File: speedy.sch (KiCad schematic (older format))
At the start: 42 parts, among them SW1 DFU, U1 STM32F415RGT6, U2 NUF2042VX6, X1 16Mhz 10ppm

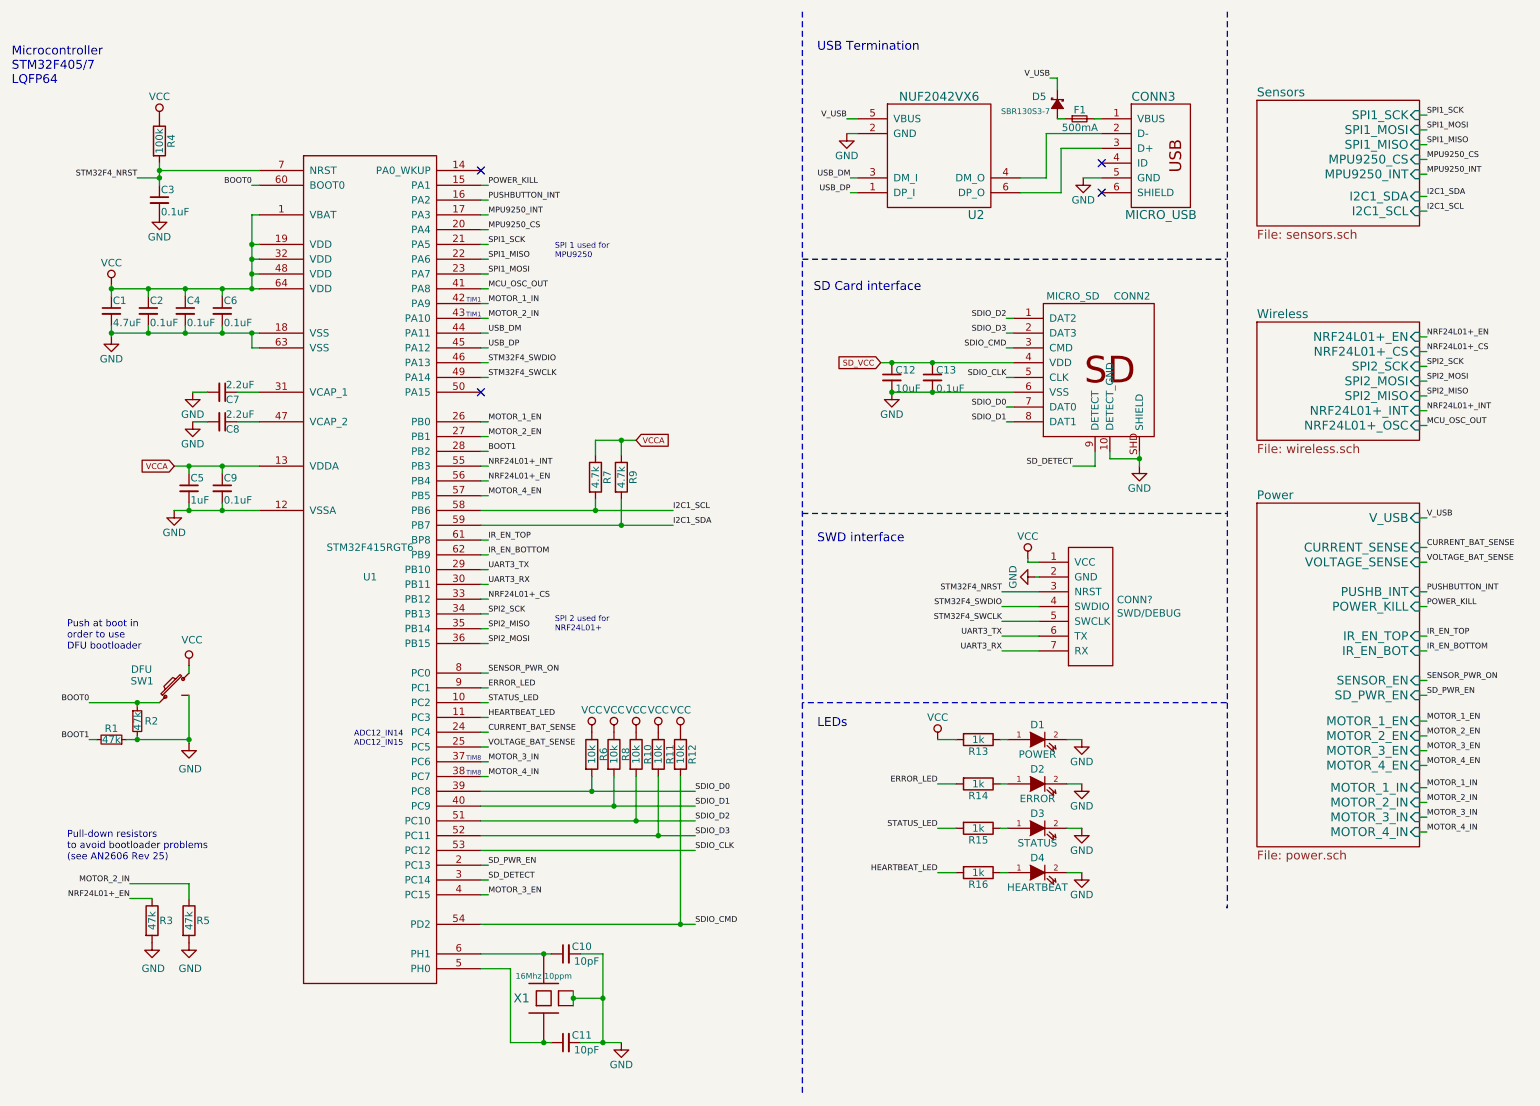
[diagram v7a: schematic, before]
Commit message: Update TOF sensor to use new ST VL53L0X with 2m range
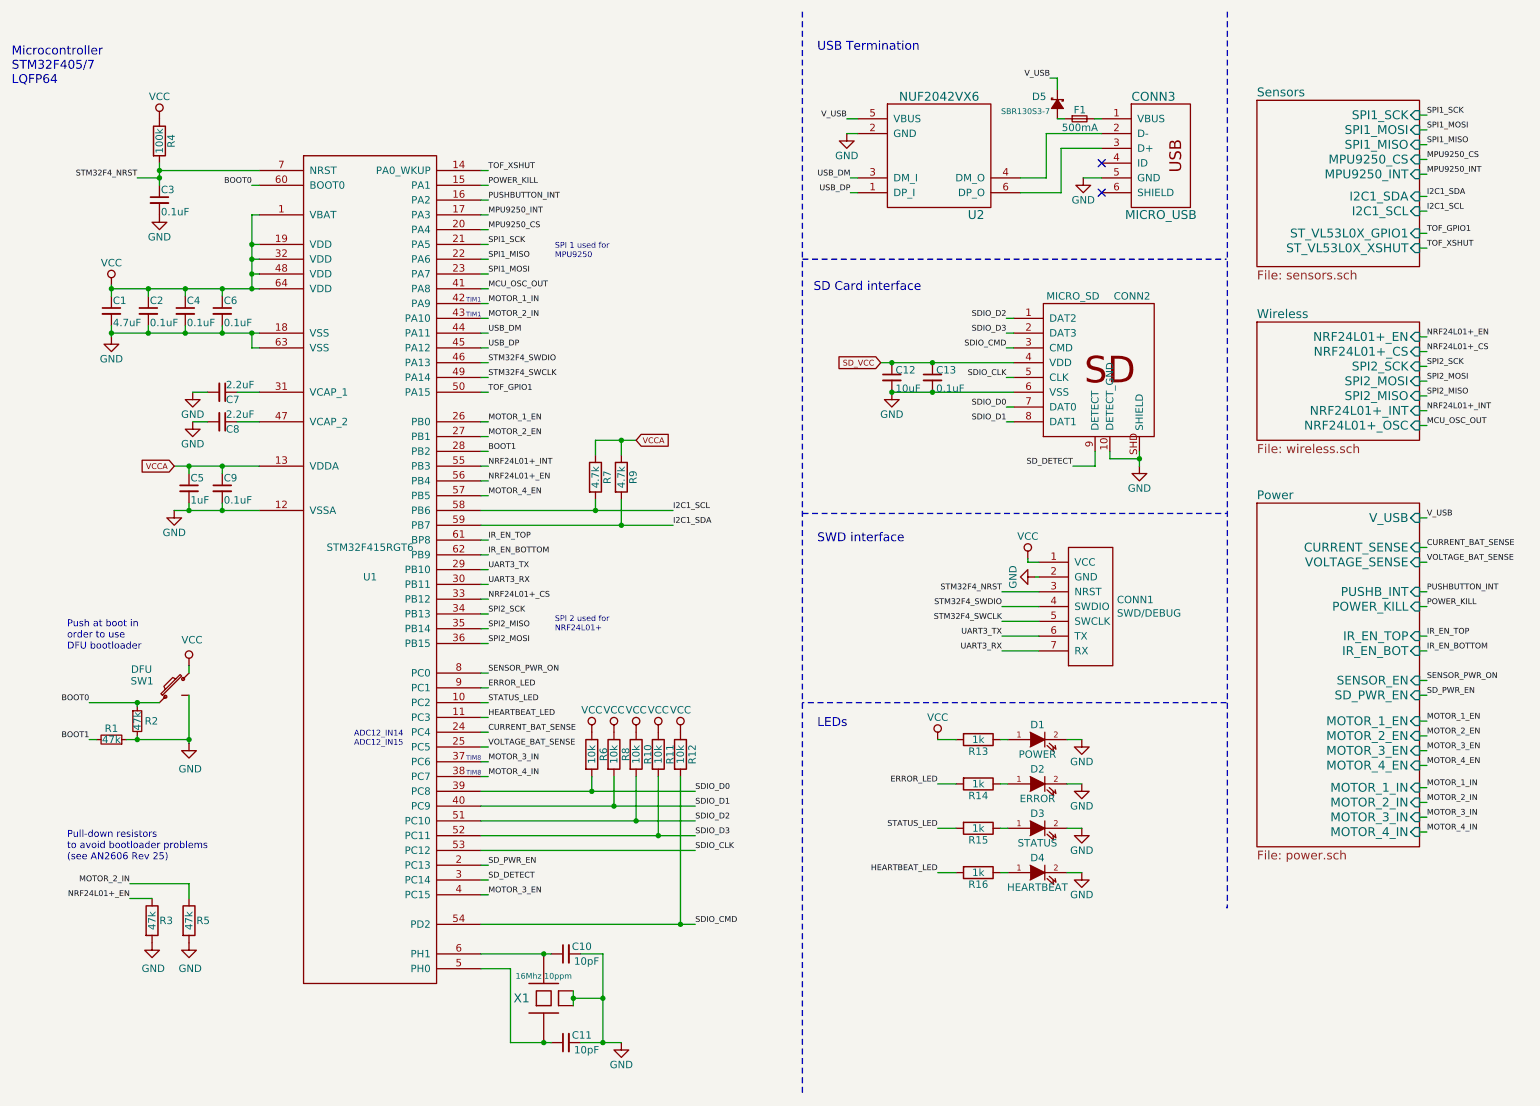
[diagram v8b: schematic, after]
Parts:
- gave numbers to parts that had none: 1
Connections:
- net TOF_XSHUT: now reaches U1.14 (PA0_WKUP)
- net TOF_GPIO1: now reaches U1.50 (PA15)
- no-connect marks 4 -> 2
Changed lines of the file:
@@
 $EndComp
 $Sheet
-S 9075 1075 1100 850
+S 9075 1075 1100 1125
 U 5536C66B
 F0 "Sensors" 60
@@
 F7 "I2C1_SCL" I R 10175 1825 60
 F8 "MPU9250_CS" I R 10175 1475 60
+F9 "ST_VL53L0X_GPIO1" I R 10175 1975 60
+F10 "ST_VL53L0X_XSHUT" I R 10175 2075 60
 $EndSheet
 Text Label 3875 1950 0    39   ~ 0
@@
 	0    -1   -1   0
 $EndComp
-NoConn ~ 3825 1550
 Text GLabel 6530 2850 0    39   Input ~ 0
 SD_VCC
@@
 Pull-down resistors \nto avoid bootloader problems \n(see AN2606 Rev 25)
 $Comp
-L SWD/DEBUG CONN?
+L SWD/DEBUG CONN1
 U 1 1 57531C38
 P 7950 4500
-F 0 "CONN?" H 8128 4546 50  0000 L CNN
+F 0 "CONN1" H 8128 4546 50  0000 L CNN
 F 1 "SWD/DEBUG" H 8128 4455 50  0000 L CNN
 F 2 "MODULE" H 7950 4450 50  0001 C CNN
@@
 Text Label 3875 2950 0    39   ~ 0
 STM32F4_SWCLK
-NoConn ~ 3825 3050
 Wire Wire Line
 	3875 3550 3825 3550
@@
 Text Label 7350 4500 2    39   ~ 0
 STM32F4_SWDIO
+Text Label 10225 1975 0    39   ~ 0
+TOF_GPIO1
+Text Label 10225 2075 0    39   ~ 0
+TOF_XSHUT
+Wire Wire Line
+	10175 2075 10225 2075
+Wire Wire Line
+	10225 1975 10175 1975
+Text Label 3875 1550 0    39   ~ 0
+TOF_XSHUT
+Wire Wire Line
+	3825 1550 3875 1550
+Text Label 3875 3050 0    39   ~ 0
+TOF_GPIO1
+Wire Wire Line
+	3875 3050 3825 3050
 $EndSCHEMATC
